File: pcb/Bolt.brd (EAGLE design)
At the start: 63.6 x 48.9 mm, 45 parts, among them J1 10118194-0001LF, Q1 XT60_YELLOW, Q2 MMSS8050-H-TP, Q3 MMSS8050-H-TP, U1 FT231XS-R, U2 ESP32-WROOM-32D, U3 LM1117DT-3.3/NOPB

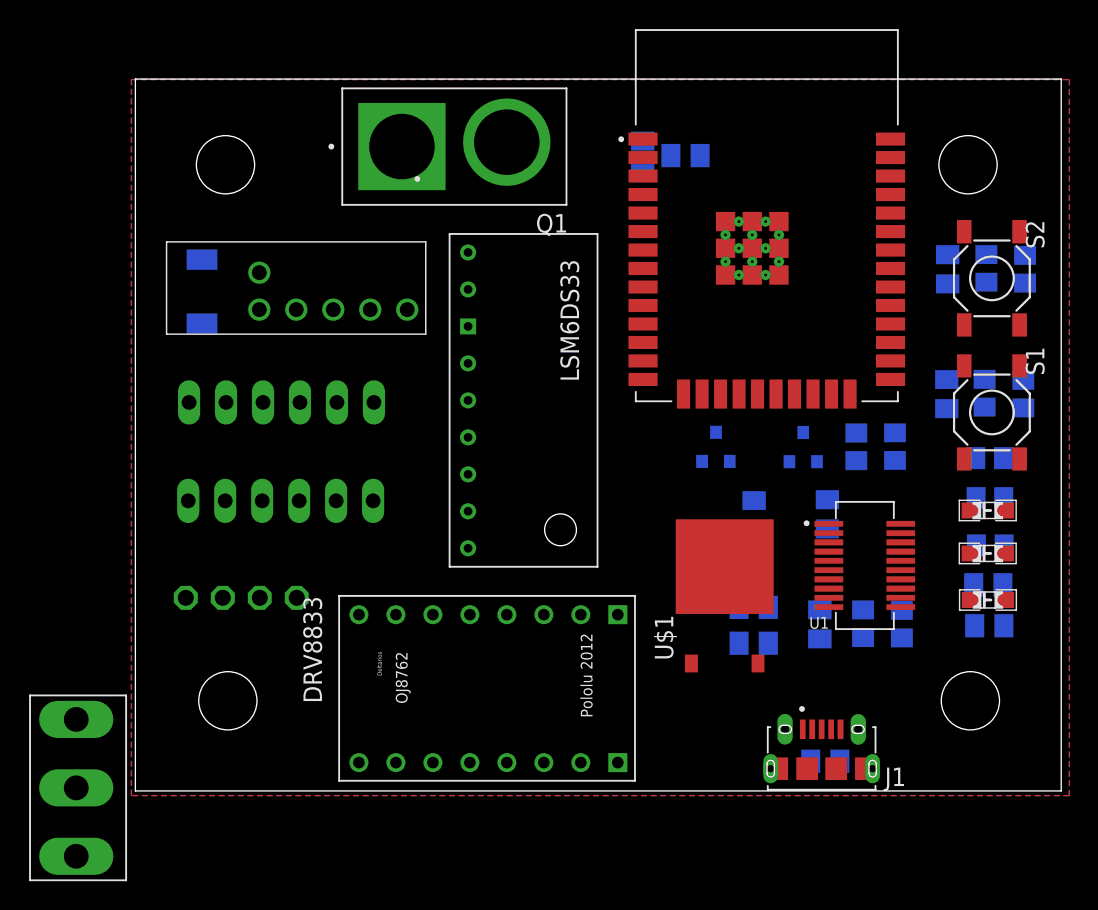
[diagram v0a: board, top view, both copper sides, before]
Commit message: Fixed removing v1.0 from the repository
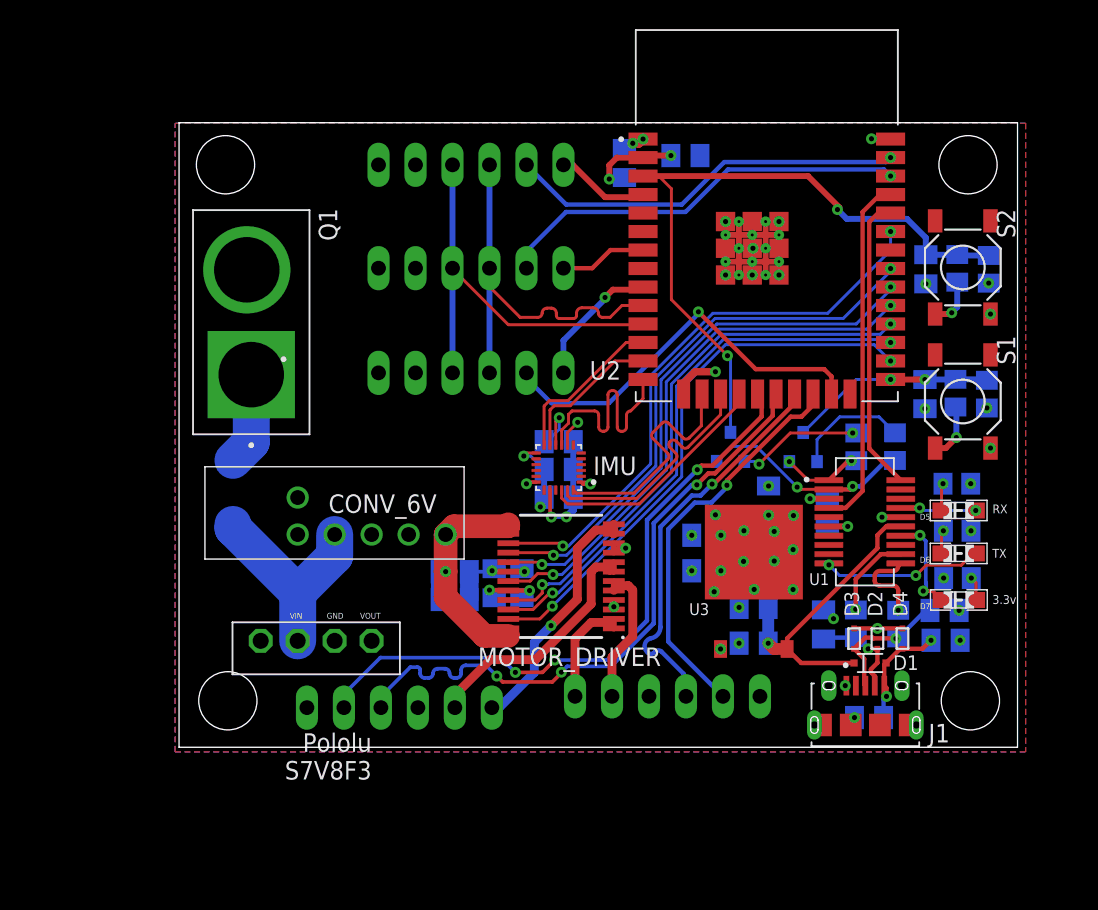
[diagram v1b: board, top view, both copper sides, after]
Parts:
- removed U$1: (no value), DRV8833:POLOLU-DRV8833
- removed U$2: POLOLU_LSM6DS33, lsm6ds33:POLOLU_LSM6DS33
- removed U$3: SWITCH, switch:SWITCH
- added C15, C17, C19, C20: 0.1uF, rcl:C0805K
- added C16, C18: 10uF, rcl:C0805K
- added C21: 10nF, rcl:C0805K
- added D1: BAT760,115, BAT760_115:SOD323(F)
- added D2, D3, D4: ESD5B5.0ST1G, ESD5B5.0ST1G:SOD-523
- added DIST_A, DIST_B, DIST_C: JST-XH-06-PIN-LONG-PAD, Rembrandt Electronics - JST XH Connectors v1-0:JST-XH-06-PACKAGE-LONG-PAD
- added IMU: MPU-9250, MPU-9250:QFN40P300X300X105-24N
- added MOTOR_DRIVER: TB6612FNG(O,C,8,EL, TB6612FNG_O_C_8_EL:SOP65P760X160-24N
- moved HALL_A 29.8 mm to (36.4, 49.5)
- moved HALL_B 22.5 mm to (17.9, 48.8), turned to 0 degrees
- moved Q1 18.4 mm to (7.77, 75.2), turned to 90 degrees
- moved CONV_6V 15.7 mm to (11.0, 63.2)
- moved D8 14.0 mm to (6.51, 63.5)
- moved CONV_3V3 5.93 mm to (12.2, 53.3), flipped to the top, turned to 180 degrees
- moved C7 4.24 mm to (50.2, 48.1)
- moved J1 4.24 mm to (49.9, 47.6)
- moved C1 3.47 mm to (55.4, 55.4)
- moved R11 3.18 mm to (56.3, 57.7)
- moved R8 3.18 mm to (56.3, 60.9)
- moved C6 3.16 mm to (55.5, 53.4)
- moved U1 3.00 mm to (49.9, 61.5)
- moved R7 2.85 mm to (56.2, 64.1)
- moved R3 2.50 mm to (58.3, 70.3)
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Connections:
- removed net N$10: U$1.GND2
- removed net N$11: U$1.VMM
- removed net N$12: U$1.INB1
- removed net N$13: U$1.INB2
- removed net N$14: U$1.INA2
- removed net N$15: U$1.INA1
- removed net N$16: U$1.SLP
- removed net N$17: U$1.FLT
- removed net N$18: U$2.VIN
- removed net N$19: U$2.SDA
- removed net N$2: U$1.GND1
- removed net N$20: U$2.SCL
- removed net N$21: U$2.SDO
- removed net N$22: U$2.CS
- removed net N$23: U$2.VDD
- removed net N$24: U$2.INT1
- removed net N$25: U$2.INT2
- removed net N$26: U$2.GND
- removed net N$27: U$3.P$1
- removed net N$29: U$3.P$2
- removed net N$3: U$1.VIN
- removed net N$30: U$3.P$3
- removed net N$4: U$1.OB1
- removed net N$5: U$1.OB2
- removed net N$6: U$1.OA2
- removed net N$7: U$1.OA1
- removed net N$8: U$1.AISEN
- removed net N$9: U$1.BINSEN
- new net REGOUT: C20.1, IMU.10
- net 6V: now also C17.1, C18.1, MOTOR_DRIVER.13, MOTOR_DRIVER.14, MOTOR_DRIVER.24
- net DIST_GPIO1_A: now also DIST_A.6
- net DIST_GPIO1_B: now also DIST_B.6
- net DIST_GPIO1_C: now also DIST_C.6
- net DIST_XSHUT_A: now also DIST_A.5
- net DIST_XSHUT_B: now also DIST_B.5
- net DIST_XSHUT_C: now also DIST_C.5
- net EXT_5V: now also D1.1; no longer J1.5
- net GND: now also C15.2, C16.2, C17.2, C18.2, C19.2, C20.2, C21.2, D2.P$2, D3.P$2, D4.P$2, DIST_A.2, DIST_B.2, DIST_C.2, IMU.18, IMU.20, MOTOR_DRIVER.10, MOTOR_DRIVER.18, MOTOR_DRIVER.3, MOTOR_DRIVER.4, MOTOR_DRIVER.9
- net I2C_SCL: now also DIST_A.4, DIST_B.4, DIST_C.4
- net I2C_SDA: now also DIST_A.3, DIST_B.3, DIST_C.3
- net IMU_CLK: now also IMU.23
- net IMU_CS: now also IMU.22
- net IMU_FSYNC: now also IMU.11
- net IMU_INT: now also IMU.12
- net IMU_SDI: now also IMU.24
- net IMU_SDO: now also IMU.9
- net M1_A: now also MOTOR_DRIVER.1, MOTOR_DRIVER.2
- net M1_B: now also MOTOR_DRIVER.11, MOTOR_DRIVER.12
- net M2_A: now also MOTOR_DRIVER.5, MOTOR_DRIVER.6
- net M2_B: now also MOTOR_DRIVER.7, MOTOR_DRIVER.8
- net M_DRV_AIN1: now also MOTOR_DRIVER.21
- net M_DRV_AIN2: now also MOTOR_DRIVER.22
- net M_DRV_BIN1: now also MOTOR_DRIVER.17
- net M_DRV_BIN2: now also MOTOR_DRIVER.16
- net M_DRV_PWMA: now also MOTOR_DRIVER.23
- net M_DRV_PWMB: now also MOTOR_DRIVER.15
- net M_DRV_STBY: now also MOTOR_DRIVER.19
- net USB_5V: now also D1.2, D4.P$1, J1.5
- net USB_DM: now also D2.P$1
- net USB_DP: now also D3.P$1
- net VCC: now also C15.1, C16.1, C19.1, C21.1, DIST_A.1, DIST_B.1, DIST_C.1, IMU.1, IMU.13, IMU.8, MOTOR_DRIVER.20
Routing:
- net GND: track 9.80 -> 76.1 mm, vias 0 -> 36
- net EN: track 0.00 -> 47.2 mm, vias 0 -> 2
- net HALL_2_B: track 0.00 -> 44.1 mm, vias 0 -> 3
- net HALL_1_B: track 0.00 -> 43.7 mm, vias 0 -> 3
- net M_DRV_PWMB: track 0.00 -> 39.6 mm, vias 0 -> 2
- net VCC: track 1.49 -> 39.8 mm, vias 0 -> 28
- net M_DRV_BIN2: track 0.00 -> 38.1 mm, vias 0 -> 2
- net M_DRV_PWMA: track 0.00 -> 38.1 mm, vias 0 -> 2
- net M_DRV_AIN1: track 0.00 -> 38.0 mm, vias 0 -> 2
- net M_DRV_BIN1: track 0.00 -> 37.9 mm, vias 0 -> 2
- net M_DRV_STBY: track 0.00 -> 37.7 mm, vias 0 -> 2
- net M_DRV_AIN2: track 0.00 -> 37.6 mm, vias 0 -> 2
- net I2C_SDA: track 0.00 -> 29.0 mm
- net DIST_XSHUT_C: track 0.00 -> 28.7 mm, vias 0 -> 1
- net I2C_SCL: track 0.00 -> 28.6 mm
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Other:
- board size 63.6 x 48.9 mm -> 57.6 x 42.9 mm
- board text added: "3.3v"
- board text added: "Bolt v1.1"
- board text added: "GND"
- board text added: "RX"
- board text added: "TX"
- board text added: "U3"
- board text added: "VIN"
- board text added: "VOUT"
